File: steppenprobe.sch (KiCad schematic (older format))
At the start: 82 parts, among them J1 USB_C_Receptacle_USB2.0, J2 Conn_ST_STDC14, J4 Conn_01x16, Q1 2N7002, SW1 SW_SPDT, SW2 SW_Push, U1 FT2232H, U10 74LVC1G125, U11 74LVC1G125, U12 74LVC1G125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

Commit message: Add a few more MPNs and tidy-up
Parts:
- C1, C17, C2, C5, C6, C7: MPN (none) -> CL10A475KO8NNNC; MPN2 CL10A475KO8NNNC -> EMK107ABJ475KA-T; Manufacturer (none) -> Samsung Electro-Mechanics; Manufacturer2 Samsung Electro-Mechanics -> Taiyo Yuden
- C10, C11, C12, C13, C14, C15, C16, C19, C20, C21, C22, C8, C9: MPN (none) -> CC0603KRX7R9BB104; MPN2 CC0603KRX7R9BB104 -> CL10B104KB8NNNC; Manufacturer (none) -> Yageo; Manufacturer2 Yageo -> Samsung Electro-Mechanics
- C18: LCSC_PN C14663 -> (none); MPN2 CC0603KRX7R9BB104 -> (none); Manufacturer2 Yageo -> (none)
- D1, D2, D3, D4, D5, D6: MPN (none) -> 19-217/GHC-YR1S2/3T; MPN2 19-217/GHC-YR1S2/3T -> 150060GS75000; Manufacturer (none) -> Everlight Elec; Manufacturer2 Everlight Elec -> Wurth Electronic
- FB1, FB2, FB3: LCSC_PN (none) -> C85831; MPN (none) -> BLM18KG121TN1D; MPN2 (none) -> BKP1608HS121-T; Manufacturer (none) -> Murata Electronics; Manufacturer2 (none) -> Taiyo Yuden
- LOGO1: value Logo_Open_Hardware_Small -> Open Source Hardware; footprint Symbol:OSHW-Logo_5.7x6mm_SilkScreen -> Symbol:OSHW-Logo_7.5x8mm_SilkScreen
- R3: LCSC_PN C25804 -> (none)
- SW2: MPN (none) -> PTS645SK43SMTR92 LFS; MPN2 (none) -> FSM2JSMAATR; Manufacturer (none) -> C&K; Manufacturer2 (none) -> TE Connectivity
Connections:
- wire segments 368 -> 367
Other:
- note removed: "Open Source Harware"

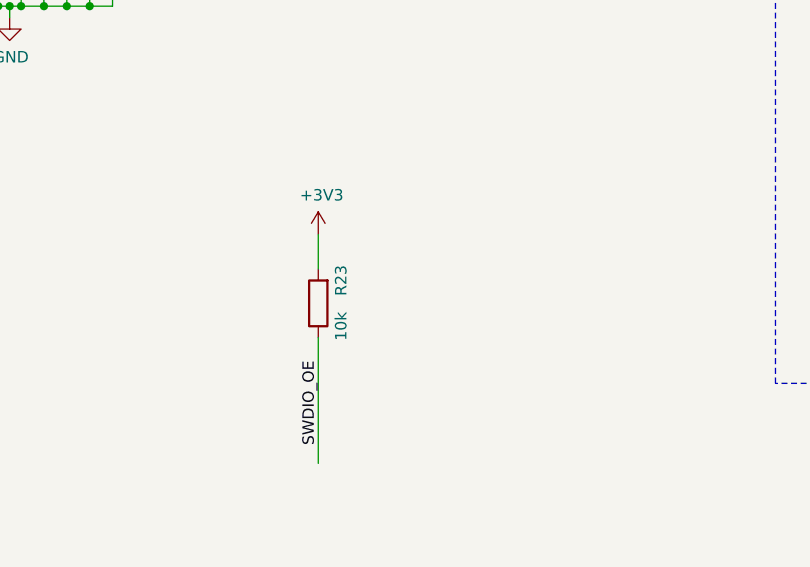
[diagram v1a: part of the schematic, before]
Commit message: Add pull down resistor to SWD_EN
I thought that the LED on that net would keep the net low when the
FTDI chip leaves reset, but the internal pull up is able to pull it
to ~2.3V. So, external pull down needed.
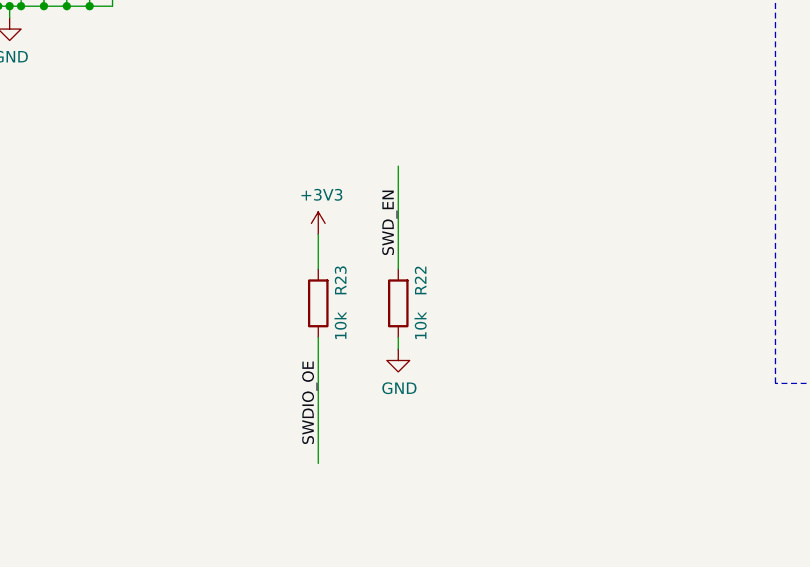
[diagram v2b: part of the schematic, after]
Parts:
- added R22: 10k, Resistor_SMD:R_0603_1608Metric, symbol Device:R
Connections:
- wire segments 367 -> 369
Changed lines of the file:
@@
 Wire Wire Line
 	8400 9650 8400 10200
-Text Label 8400 9750 3    50   ~ 0
-SWDIO_OE
 Wire Wire Line
 	8400 9200 8400 9350
@@
 	1    0    0    -1
 $EndComp
+$Comp
+L Device:R R22
+U 1 1 5DF52301
+P 8750 9500
+F 0 "R22" V 8650 9400 50  0000 C CNN
+F 1 "10k" V 8650 9600 50  0000 C CNN
+F 2 "Resistor_SMD:R_0603_1608Metric" V 8680 9500 50  0001 C CNN
+F 3 "~" H 8750 9500 50  0001 C CNN
+F 4 "C25804" H 8750 9500 50  0001 C CNN "LCSC_PN"
+	1    8750 9500
+	-1   0    0    1
+$EndComp
+Wire Wire Line
+	8750 9650 8750 9700
+$Comp
+L power:GND #PWR065
+U 1 1 5DF533AF
+P 8750 9700
+F 0 "#PWR065" H 8750 9450 50  0001 C CNN
+F 1 "GND" H 8755 9527 50  0000 C CNN
+F 2 "" H 8750 9700 50  0001 C CNN
+F 3 "" H 8750 9700 50  0001 C CNN
+	1    8750 9700
+	1    0    0    -1
+$EndComp
+Wire Wire Line
+	8750 9350 8750 8900
+Text Label 8400 9750 3    50   ~ 0
+SWDIO_OE
+Text Label 8750 9000 3    50   ~ 0
+SWD_EN
 $EndSCHEMATC

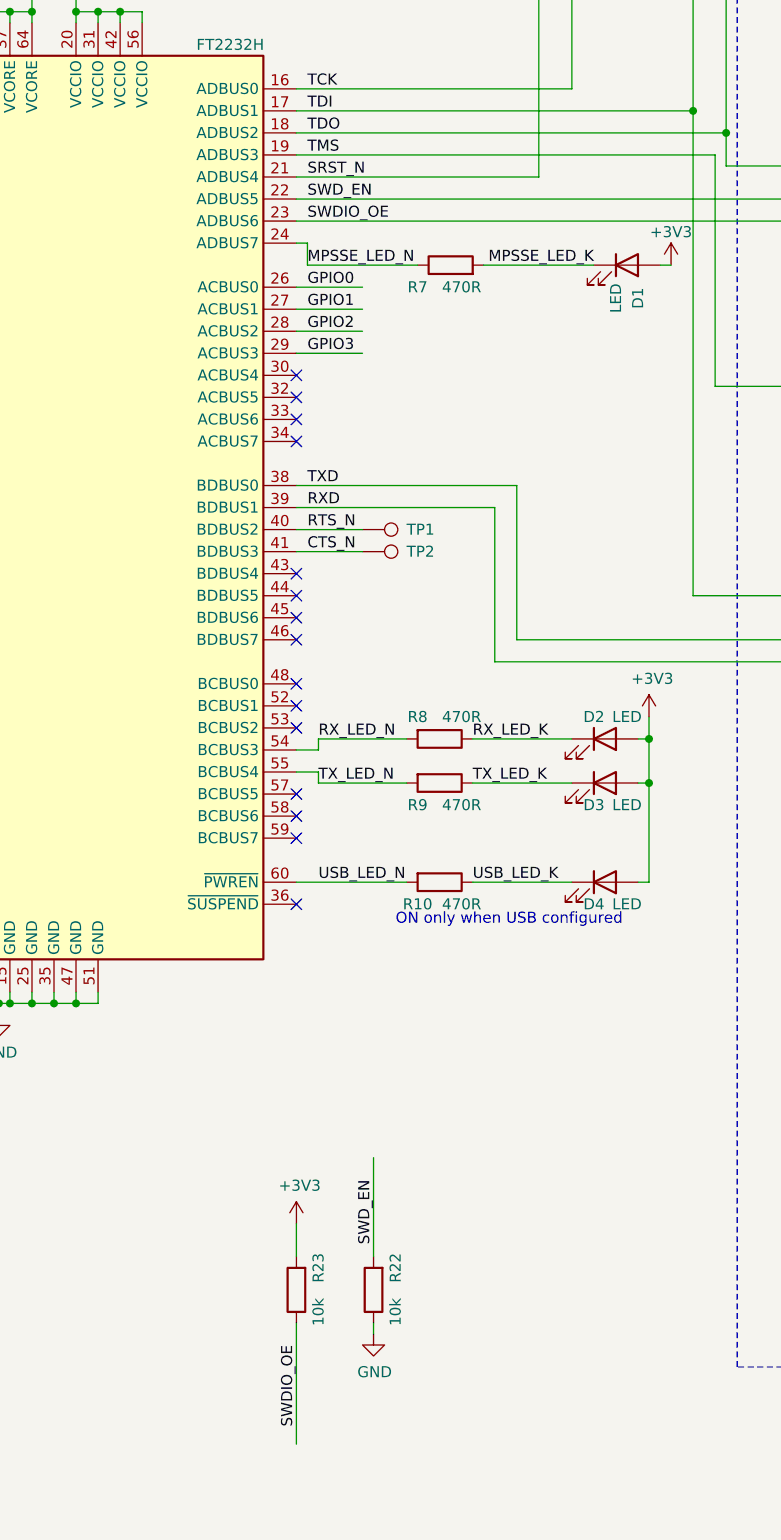
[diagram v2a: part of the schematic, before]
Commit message: Add pulldown to SRST (also rename from SRST_N)
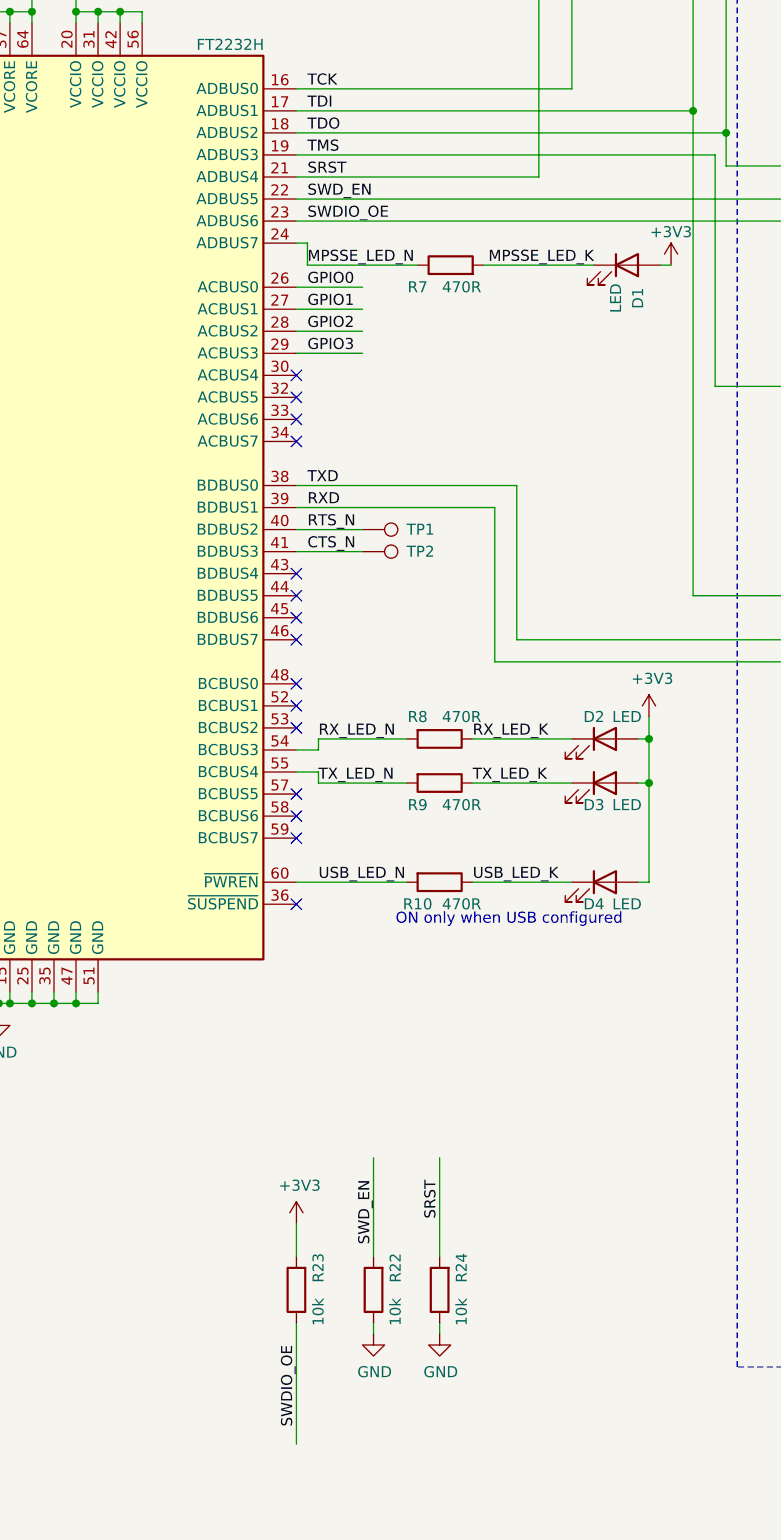
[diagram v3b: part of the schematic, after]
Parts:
- added R24: 10k, Resistor_SMD:R_0603_1608Metric, symbol Device:R
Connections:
- net labels added: SRST
- net labels removed: SRST_N
- wire segments 369 -> 371
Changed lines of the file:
@@
 TMS
 Text Label 8450 4450 0    50   ~ 0
-SRST_N
+SRST
 Text Label 8450 5850 0    50   ~ 0
 TXD
@@
 Text Label 8750 9000 3    50   ~ 0
 SWD_EN
+Wire Wire Line
+	9050 9650 9050 9700
+$Comp
+L Device:R R24
+U 1 1 5DF55E92
+P 9050 9500
+F 0 "R24" V 8950 9400 50  0000 C CNN
+F 1 "10k" V 8950 9600 50  0000 C CNN
+F 2 "Resistor_SMD:R_0603_1608Metric" V 8980 9500 50  0001 C CNN
+F 3 "~" H 9050 9500 50  0001 C CNN
+F 4 "C25804" H 9050 9500 50  0001 C CNN "LCSC_PN"
+	1    9050 9500
+	-1   0    0    1
+$EndComp
+Wire Wire Line
+	9050 9350 9050 8900
+$Comp
+L power:GND #PWR066
+U 1 1 5DF55EA1
+P 9050 9700
+F 0 "#PWR066" H 9050 9450 50  0001 C CNN
+F 1 "GND" H 9055 9527 50  0000 C CNN
+F 2 "" H 9050 9700 50  0001 C CNN
+F 3 "" H 9050 9700 50  0001 C CNN
+	1    9050 9700
+	1    0    0    -1
+$EndComp
+Text Label 9050 9000 3    50   ~ 0
+SRST
 $EndSCHEMATC

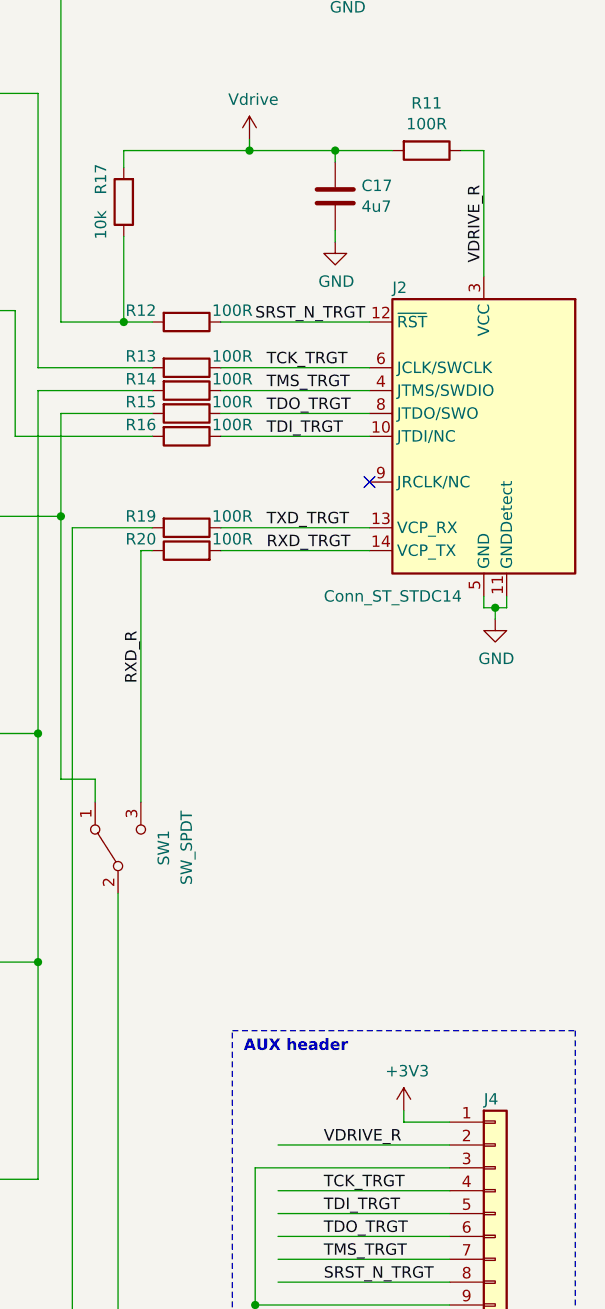
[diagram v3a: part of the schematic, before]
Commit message: Rename VDRIVE_R to VDRIVE_TRGT
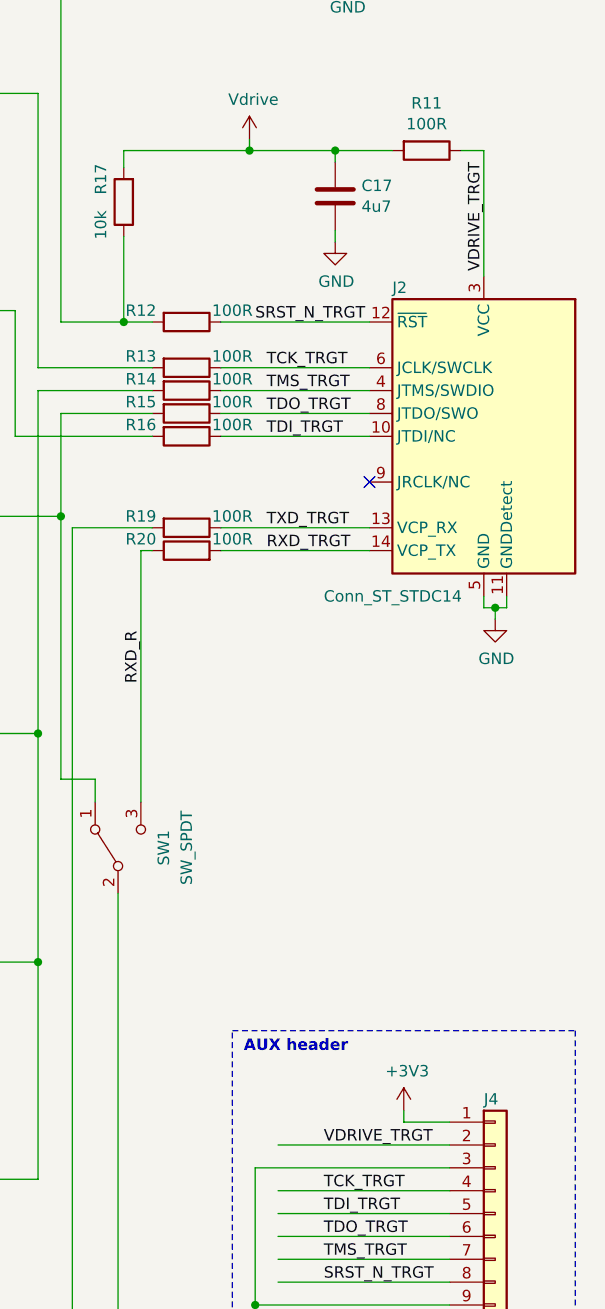
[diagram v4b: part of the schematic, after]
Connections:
- net labels added: VDRIVE_TRGT
- net labels removed: VDRIVE_R
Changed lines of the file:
@@
 Text Label 12750 3450 0    50   ~ 0
 TDO_R
-Text Label 15600 2000 3    50   ~ 0
-VDRIVE_R
+Text Label 15600 1900 3    50   ~ 0
+VDRIVE_TRGT
 Wire Wire Line
 	15500 1850 15600 1850
@@
 	14700 6200 15450 6200
 Text Label 14900 6200 0    50   ~ 0
-VDRIVE_R
+VDRIVE_TRGT
 Wire Wire Line
 	14600 7600 15450 7600

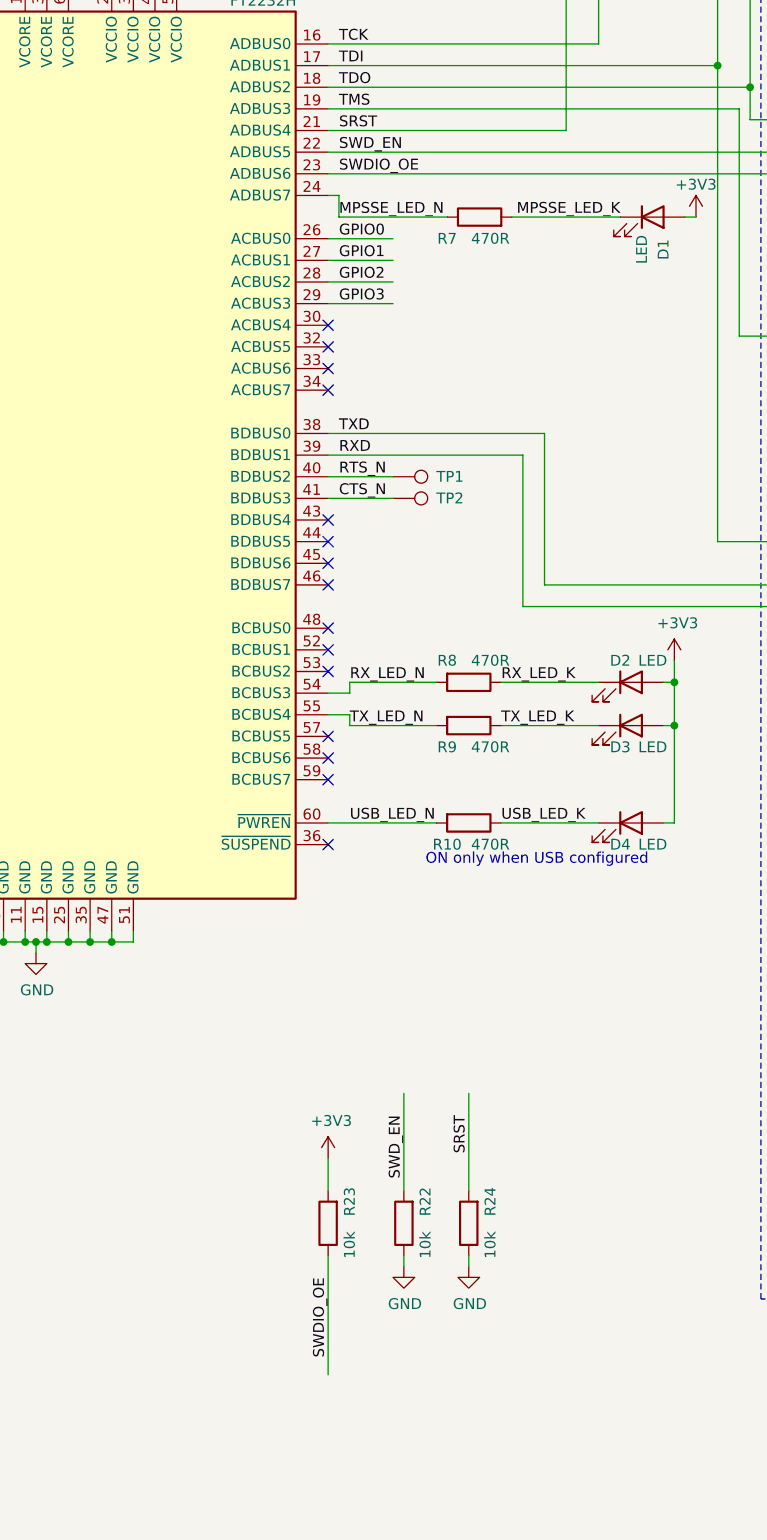
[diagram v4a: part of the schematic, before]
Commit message: Rename SWDIO_OE to SWDIO_OE_N
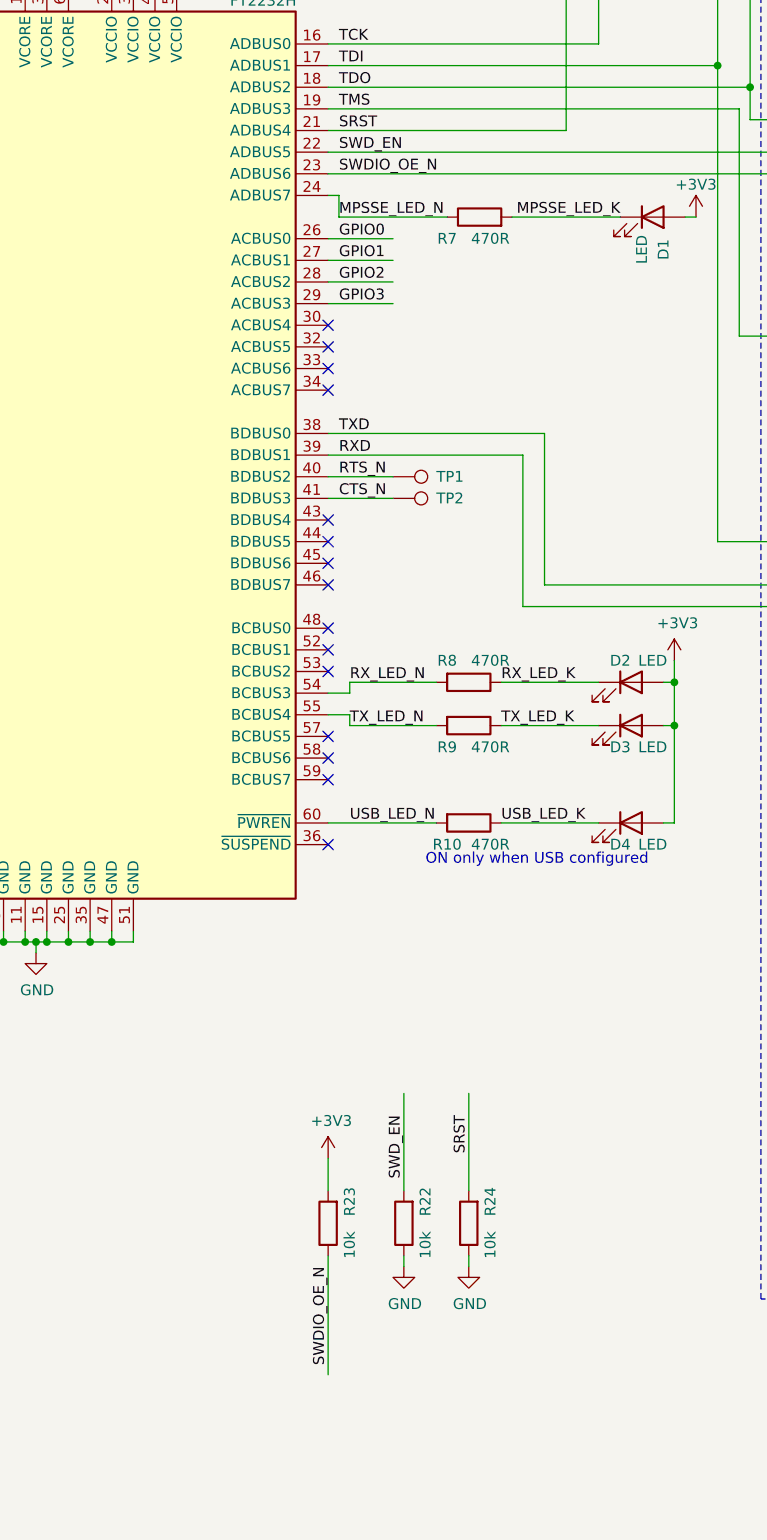
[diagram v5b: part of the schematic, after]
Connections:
- net labels added: SWDIO_OE_N
- net labels removed: SWDIO_OE
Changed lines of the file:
@@
 SWD_EN
 Text Label 8450 4650 0    50   ~ 0
-SWDIO_OE
+SWDIO_OE_N
 Wire Wire Line
 	8400 4150 10200 4150
@@
 Wire Wire Line
 	8750 9350 8750 8900
-Text Label 8400 9750 3    50   ~ 0
-SWDIO_OE
+Text Label 8400 9700 3    50   ~ 0
+SWDIO_OE_N
 Text Label 8750 9000 3    50   ~ 0
 SWD_EN

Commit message: Tidy-up schematic.
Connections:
- wire segments 371 -> 372
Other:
- note added: "Arm Cortex Debug + UART"
- note added: "BUFFERS"
- note added: "STDC14 connector"
- moved on the sheet: C17, C19, C20, C21, J2, Q1, R11, R12, R13, R14, R15, R16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
